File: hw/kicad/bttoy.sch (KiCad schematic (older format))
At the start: 28 parts

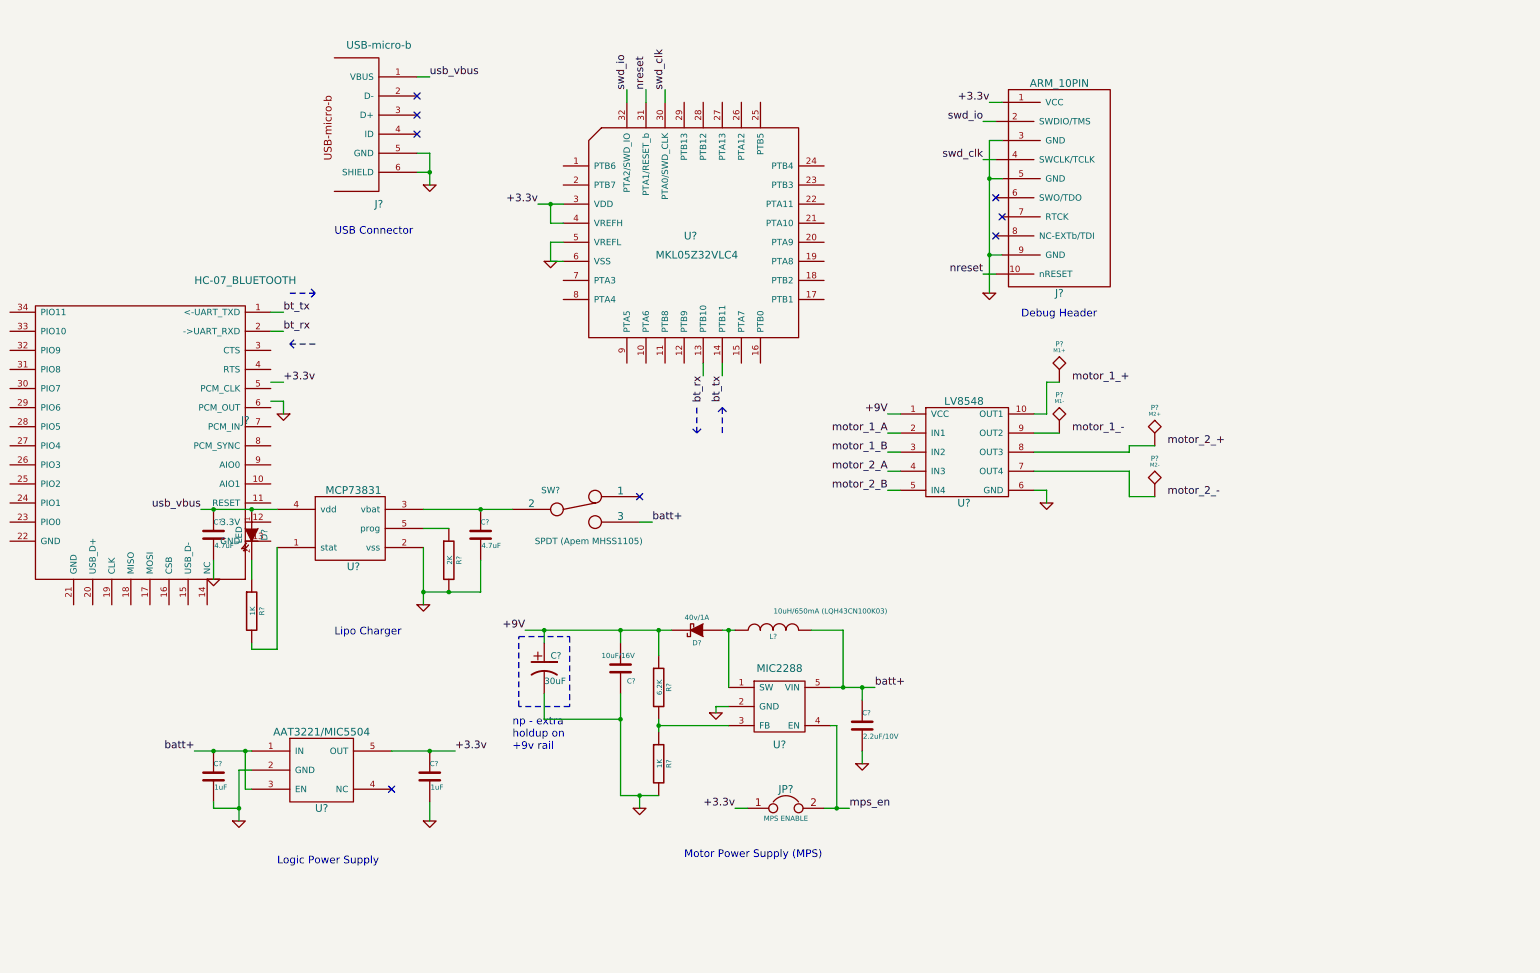
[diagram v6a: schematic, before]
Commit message: - fill out motor control subsystem
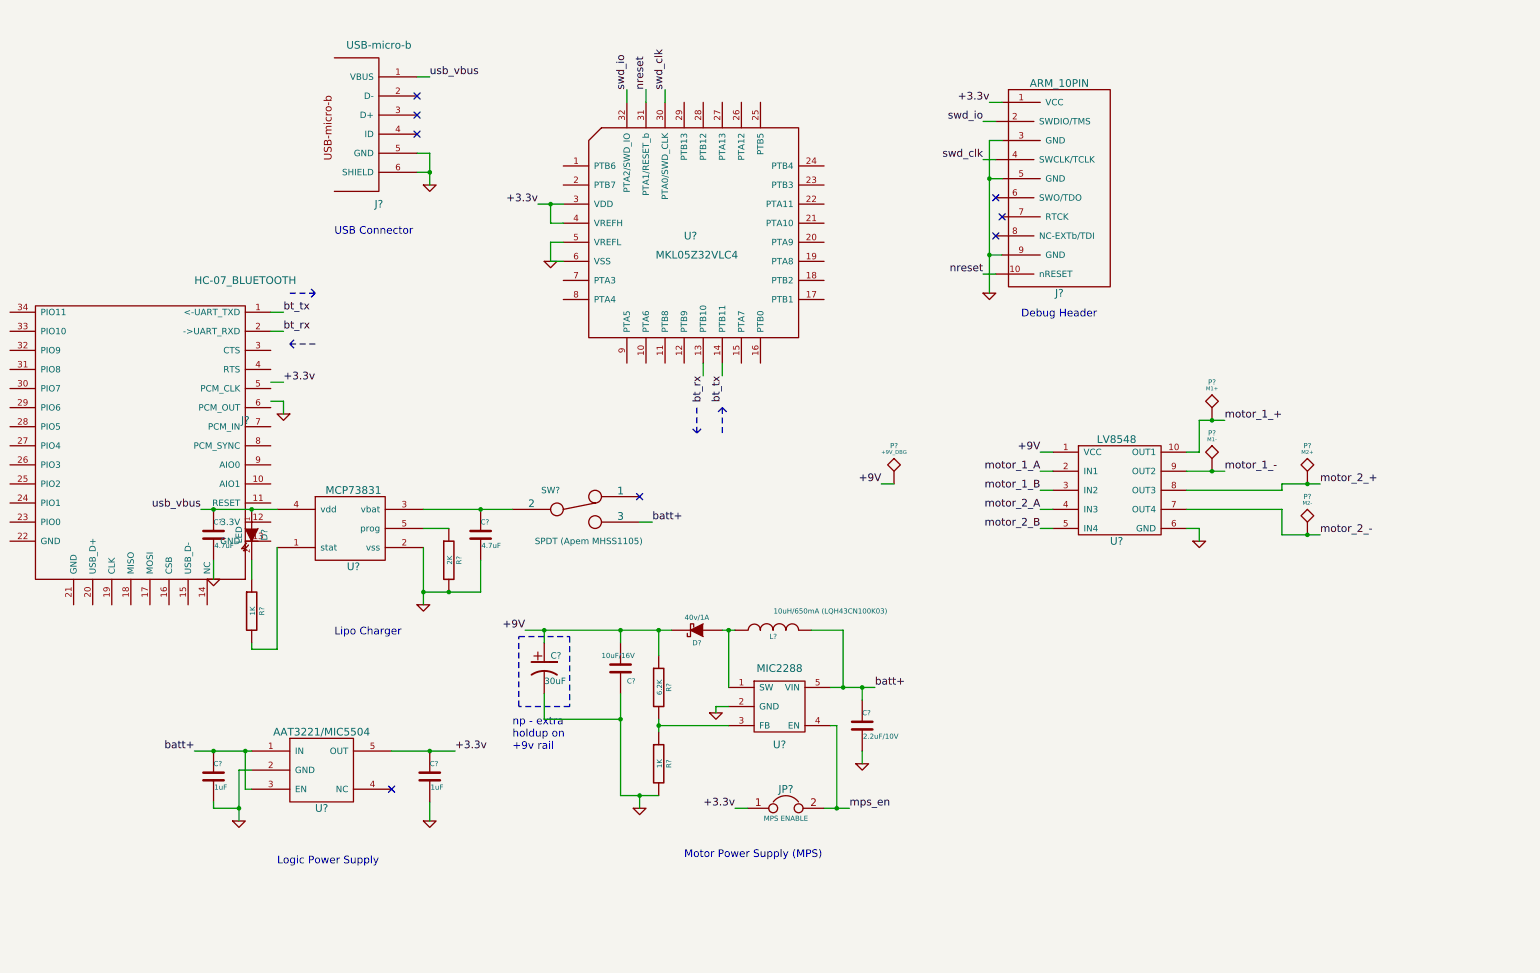
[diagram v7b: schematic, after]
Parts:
- added P?: +9V_DBG, symbol TST
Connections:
- net +9V: now also P?.1
- net motor_1_+: now also P?.1, U?.10 (OUT1)
- net motor_1_-: now also P?.1, U?.9 (OUT2)
- net motor_2_+: now also P?.1, U?.8 (OUT3)
- net motor_2_-: now also P?.1, U?.7 (OUT4)
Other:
- moved on the sheet: P?, U?
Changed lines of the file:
@@
 	1    0    0    -1
 $EndComp
-Text Label 6350 4000 2    60   ~ 0
+Text Label 7550 4300 2    60   ~ 0
 motor_2_A
-Text Label 6350 4150 2    60   ~ 0
+Text Label 7550 4450 2    60   ~ 0
 motor_2_B
 $Comp
@@
 Text Label 5050 3250 3    60   ~ 0
 bt_tx
-Text Label 6350 3700 2    60   ~ 0
+Text Label 7550 4000 2    60   ~ 0
 motor_1_A
-Text Label 6350 3850 2    60   ~ 0
+Text Label 7550 4150 2    60   ~ 0
 motor_1_B
 $Comp
 L LV8548 U?
 U 1 1 54FC62AA
-P 6950 3800
-F 0 "U?" H 6950 3350 60  0000 C CNN
-F 1 "LV8548" H 6950 4150 60  0000 C CNN
-F 2 "" H 6850 3800 60  0000 C CNN
-F 3 "" H 6850 3800 60  0000 C CNN
-	1    6950 3800
+P 8150 4100
+F 0 "U?" H 8150 3650 60  0000 C CNN
+F 1 "LV8548" H 8150 4450 60  0000 C CNN
+F 2 "" H 8050 4100 60  0000 C CNN
+F 3 "" H 8050 4100 60  0000 C CNN
+	1    8150 4100
 	1    0    0    -1
 $EndComp
@@
 L GND #PWR?
 U 1 1 54FC64F5
-P 7600 4250
-F 0 "#PWR?" H 7600 4250 30  0001 C CNN
-F 1 "GND" H 7600 4180 30  0001 C CNN
-F 2 "" H 7600 4250 60  0000 C CNN
-F 3 "" H 7600 4250 60  0000 C CNN
-	1    7600 4250
-	1    0    0    -1
-$EndComp
-Text Label 6350 3550 2    60   ~ 0
+P 8800 4550
+F 0 "#PWR?" H 8800 4550 30  0001 C CNN
+F 1 "GND" H 8800 4480 30  0001 C CNN
+F 2 "" H 8800 4550 60  0000 C CNN
+F 3 "" H 8800 4550 60  0000 C CNN
+	1    8800 4550
+	1    0    0    -1
+$EndComp
+Text Label 7550 3850 2    60   ~ 0
 +9V
+$Comp
+L TST P?
+U 1 1 54FC793F
+P 8900 3600
+F 0 "P?" H 8900 3900 40  0000 C CNN
+F 1 "M1+" H 8900 3850 30  0000 C CNN
+F 2 "" H 8900 3600 60  0000 C CNN
+F 3 "" H 8900 3600 60  0000 C CNN
+	1    8900 3600
+	1    0    0    -1
+$EndComp
+Text Label 9000 3600 0    60   ~ 0
+motor_1_+
+Text Label 9000 4000 0    60   ~ 0
+motor_1_-
+Text Label 9750 4100 0    60   ~ 0
+motor_2_+
+Text Label 9750 4500 0    60   ~ 0
+motor_2_-
+$Comp
+L TST P?
+U 1 1 54FC7D5F
+P 8900 4000
+F 0 "P?" H 8900 4300 40  0000 C CNN
+F 1 "M1-" H 8900 4250 30  0000 C CNN
+F 2 "" H 8900 4000 60  0000 C CNN
+F 3 "" H 8900 4000 60  0000 C CNN
+	1    8900 4000
+	1    0    0    -1
+$EndComp
+$Comp
+L TST P?
+U 1 1 54FC7D8F
+P 9650 4100
+F 0 "P?" H 9650 4400 40  0000 C CNN
+F 1 "M2+" H 9650 4350 30  0000 C CNN
+F 2 "" H 9650 4100 60  0000 C CNN
+F 3 "" H 9650 4100 60  0000 C CNN
+	1    9650 4100
+	1    0    0    -1
+$EndComp
+$Comp
+L TST P?
+U 1 1 54FC7DC0
+P 9650 4500
+F 0 "P?" H 9650 4800 40  0000 C CNN
+F 1 "M2-" H 9650 4750 30  0000 C CNN
+F 2 "" H 9650 4500 60  0000 C CNN
+F 3 "" H 9650 4500 60  0000 C CNN
+	1    9650 4500
+	1    0    0    -1
+$EndComp
 Wire Wire Line
 	1550 4600 1550 5400
@@
 	2900 4450 2700 4450
 Wire Wire Line
-	2700 4300 3150 4300
-Wire Wire Line
-	3150 4300 3400 4300
+	2700 4300 3400 4300
 Connection ~ 1350 4300
 Wire Wire Line
 	1050 4850 1050 4700
 Wire Wire Line
-	2700 4600 2700 4950
-Wire Wire Line
-	2700 4950 2700 5050
-Wire Wire Line
-	2700 4950 2900 4950
-Wire Wire Line
-	2900 4950 3150 4950
+	2700 4600 2700 5050
+Wire Wire Line
+	2700 4950 3150 4950
 Connection ~ 2700 4950
 Wire Wire Line
@@
 	2650 900  2750 900
 Wire Wire Line
-	2750 1500 2750 1650
-Wire Wire Line
-	2750 1650 2750 1750
+	2750 1500 2750 1750
 Wire Wire Line
 	2750 1650 2650 1650
@@
 Connection ~ 2750 1650
 Wire Wire Line
-	2450 6200 2750 6200
-Wire Wire Line
-	2750 6200 2950 6200
-Wire Wire Line
-	900  6200 1050 6200
-Wire Wire Line
-	1050 6200 1300 6200
-Wire Wire Line
-	1300 6200 1350 6200
-Wire Wire Line
-	1250 6350 1250 6650
-Wire Wire Line
-	1250 6650 1250 6750
+	2450 6200 2950 6200
+Wire Wire Line
+	900  6200 1350 6200
+Wire Wire Line
+	1250 6350 1250 6750
 Wire Wire Line
 	1250 6350 1350 6350
@@
 	3700 2350 3800 2350
 Wire Wire Line
-	3600 1900 3700 1900
-Wire Wire Line
-	3700 1900 3800 1900
+	3600 1900 3800 1900
 Wire Wire Line
 	7150 2300 7250 2300
 Wire Wire Line
-	7150 1400 7150 1700
-Wire Wire Line
-	7150 1700 7150 2300
-Wire Wire Line
-	7150 2300 7150 2600
+	7150 1400 7150 2600
 Wire Wire Line
 	7150 1700 7250 1700
@@
 	7100 2450 7200 2450
 Wire Wire Line
-	950  4300 1050 4300
-Wire Wire Line
-	1050 4300 1350 4300
-Wire Wire Line
-	1350 4300 1550 4300
+	950  4300 1550 4300
 Connection ~ 1050 4300
 Wire Wire Line
-	5900 5700 6000 5700
-Wire Wire Line
-	6000 5700 6150 5700
-Wire Wire Line
-	6150 5700 6250 5700
-Wire Wire Line
-	5050 5250 5100 5250
-Wire Wire Line
-	5100 5250 5150 5250
+	5900 5700 6250 5700
+Wire Wire Line
+	5050 5250 5150 5250
 Wire Wire Line
 	6150 5800 6150 5700
@@
 	6150 6300 6150 6200
 Wire Wire Line
-	3500 5250 3650 5250
-Wire Wire Line
-	3650 5250 4250 5250
-Wire Wire Line
-	4250 5250 4550 5250
-Wire Wire Line
-	4550 5250 4650 5250
-Wire Wire Line
-	4250 5750 4250 5950
-Wire Wire Line
-	4250 5950 4250 6550
+	3500 5250 4650 5250
+Wire Wire Line
+	4250 5750 4250 6550
 Wire Wire Line
 	4550 5250 4550 5450
@@
 	4250 5350 4250 5250
 Wire Wire Line
-	4550 5950 4550 6000
-Wire Wire Line
-	4550 6000 4550 6050
-Wire Wire Line
-	4250 6550 4400 6550
-Wire Wire Line
-	4400 6550 4550 6550
+	4550 5950 4550 6050
+Wire Wire Line
+	4250 6550 4550 6550
 Wire Wire Line
 	4400 6550 4400 6650
@@
 	5150 6650 5250 6650
 Wire Wire Line
-	5850 6650 5950 6650
-Wire Wire Line
-	5950 6650 6050 6650
+	5850 6650 6050 6650
 Wire Wire Line
 	5950 6650 5950 6000
@@
 	5050 3250 5050 3150
 Wire Wire Line
-	6350 3550 6450 3550
-Wire Wire Line
-	7500 4150 7600 4150
-Wire Wire Line
-	7600 4150 7600 4250
-Wire Wire Line
-	6350 3700 6450 3700
-Wire Wire Line
-	6350 3850 6450 3850
-Wire Wire Line
-	6450 4000 6350 4000
-Wire Wire Line
-	6350 4150 6450 4150
+	7550 3850 7650 3850
+Wire Wire Line
+	8700 4450 8800 4450
+Wire Wire Line
+	8800 4450 8800 4550
+Wire Wire Line
+	7550 4000 7650 4000
+Wire Wire Line
+	7550 4150 7650 4150
+Wire Wire Line
+	7650 4300 7550 4300
+Wire Wire Line
+	7550 4450 7650 4450
+Wire Wire Line
+	8700 3850 8800 3850
+Wire Wire Line
+	8800 3850 8800 3600
+Wire Wire Line
+	8800 3600 9000 3600
+Wire Wire Line
+	8700 4000 9000 4000
+Wire Wire Line
+	8700 4150 9450 4150
+Wire Wire Line
+	9450 4150 9450 4100
+Wire Wire Line
+	9450 4100 9750 4100
+Wire Wire Line
+	8700 4300 9450 4300
+Wire Wire Line
+	9450 4300 9450 4500
+Wire Wire Line
+	9450 4500 9750 4500
+Connection ~ 8900 3600
+Connection ~ 9650 4100
+Connection ~ 8900 4000
+Connection ~ 9650 4500
+Text Label 6300 4100 2    60   ~ 0
++9V
 $Comp
 L TST P?
-U 1 1 54FC793F
-P 7700 3300
-F 0 "P?" H 7700 3600 40  0000 C CNN
-F 1 "M1+" H 7700 3550 30  0000 C CNN
-F 2 "" H 7700 3300 60  0000 C CNN
-F 3 "" H 7700 3300 60  0000 C CNN
-	1    7700 3300
-	1    0    0    -1
-$EndComp
-Text Label 7800 3300 0    60   ~ 0
-motor_1_+
-Text Label 7800 3700 0    60   ~ 0
-motor_1_-
-Text Label 8550 3800 0    60   ~ 0
-motor_2_+
-Text Label 8550 4200 0    60   ~ 0
-motor_2_-
-$Comp
-L TST P?
-U 1 1 54FC7D5F
-P 7700 3700
-F 0 "P?" H 7700 4000 40  0000 C CNN
-F 1 "M1-" H 7700 3950 30  0000 C CNN
-F 2 "" H 7700 3700 60  0000 C CNN
-F 3 "" H 7700 3700 60  0000 C CNN
-	1    7700 3700
-	1    0    0    -1
-$EndComp
-$Comp
-L TST P?
-U 1 1 54FC7D8F
-P 8450 3800
-F 0 "P?" H 8450 4100 40  0000 C CNN
-F 1 "M2+" H 8450 4050 30  0000 C CNN
-F 2 "" H 8450 3800 60  0000 C CNN
-F 3 "" H 8450 3800 60  0000 C CNN
-	1    8450 3800
-	1    0    0    -1
-$EndComp
-$Comp
-L TST P?
-U 1 1 54FC7DC0
-P 8450 4200
-F 0 "P?" H 8450 4500 40  0000 C CNN
-F 1 "M2-" H 8450 4450 30  0000 C CNN
-F 2 "" H 8450 4200 60  0000 C CNN
-F 3 "" H 8450 4200 60  0000 C CNN
-	1    8450 4200
-	1    0    0    -1
-$EndComp
-Wire Wire Line
-	7500 3550 7600 3550
-Wire Wire Line
-	7600 3550 7600 3300
-Wire Wire Line
-	7600 3300 7700 3300
-Wire Wire Line
-	7500 3700 7700 3700
-Wire Wire Line
-	7500 3850 8250 3850
-Wire Wire Line
-	8250 3850 8250 3800
-Wire Wire Line
-	8250 3800 8450 3800
-Wire Wire Line
-	7500 4000 8250 4000
-Wire Wire Line
-	8250 4000 8250 4200
-Wire Wire Line
-	8250 4200 8450 4200
+U 1 1 54FCC050
+P 6400 4100
+F 0 "P?" H 6400 4400 40  0000 C CNN
+F 1 "+9V_DBG" H 6400 4350 30  0000 C CNN
+F 2 "" H 6400 4100 60  0000 C CNN
+F 3 "" H 6400 4100 60  0000 C CNN
+	1    6400 4100
+	1    0    0    -1
+$EndComp
+Wire Wire Line
+	6400 4100 6300 4100
 $EndSCHEMATC

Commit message: - more work on schematic
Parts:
- added D? (x3): LED, symbol LED
- added R? (x3): 1K, symbol R
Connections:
- net +3.3v: now also J?.12 (3.3V)
- net GND: now also J?.13 (GND), J?.21 (GND), J?.22 (GND)
- new net: D?.2 (K), R?.1 (x3)
- no-connect marks 8 -> 36
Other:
- note added: "Motor Control"
- moved on the sheet: C?, D?, J?, JP?, L?, P?, R?, SW?, U?
